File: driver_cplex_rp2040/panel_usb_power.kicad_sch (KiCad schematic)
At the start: 7 parts, among them J5 USB_C_Receptacle_USB2.0, U2 AP2112K-3.3

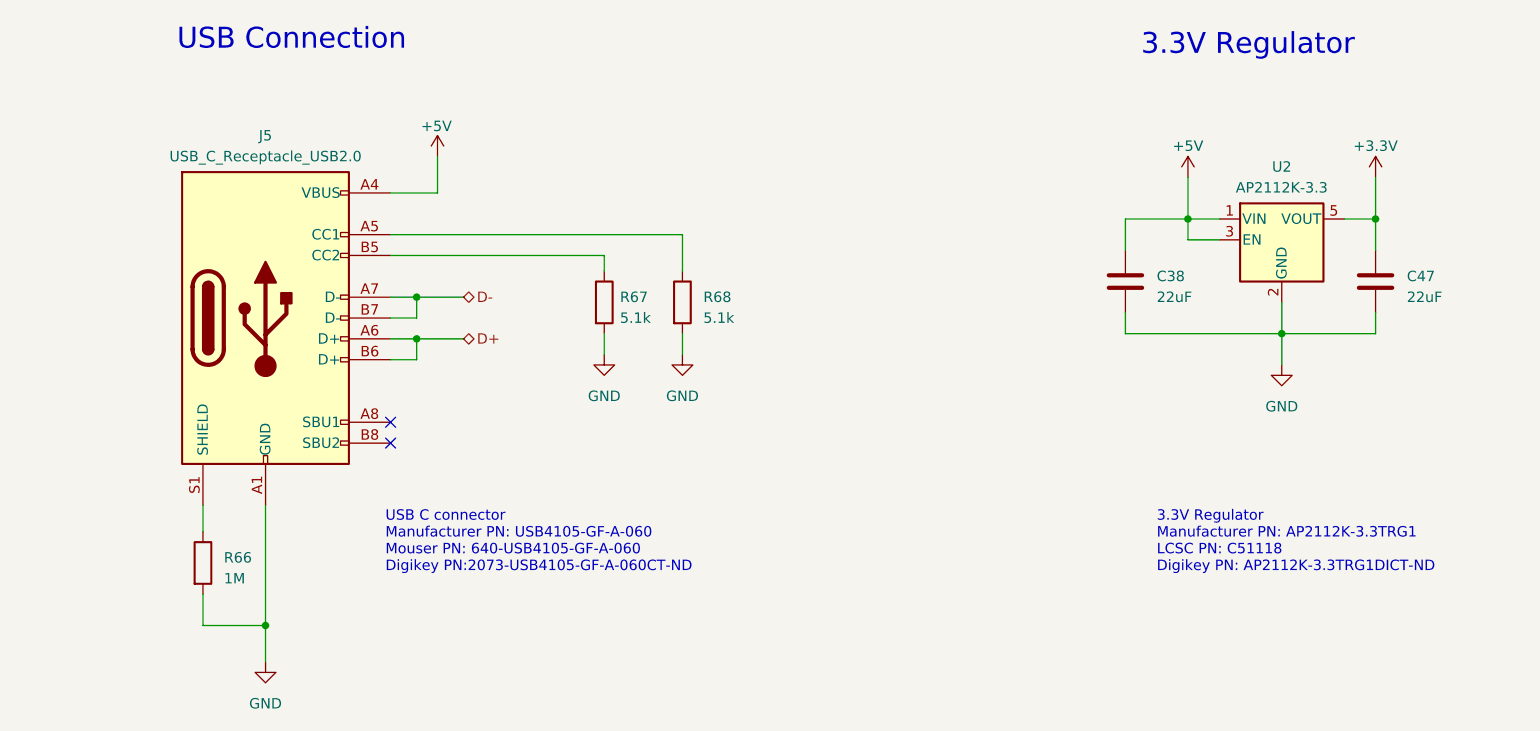
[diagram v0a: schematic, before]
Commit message: Added Charlieplexed version of rp2040 single pcb design.
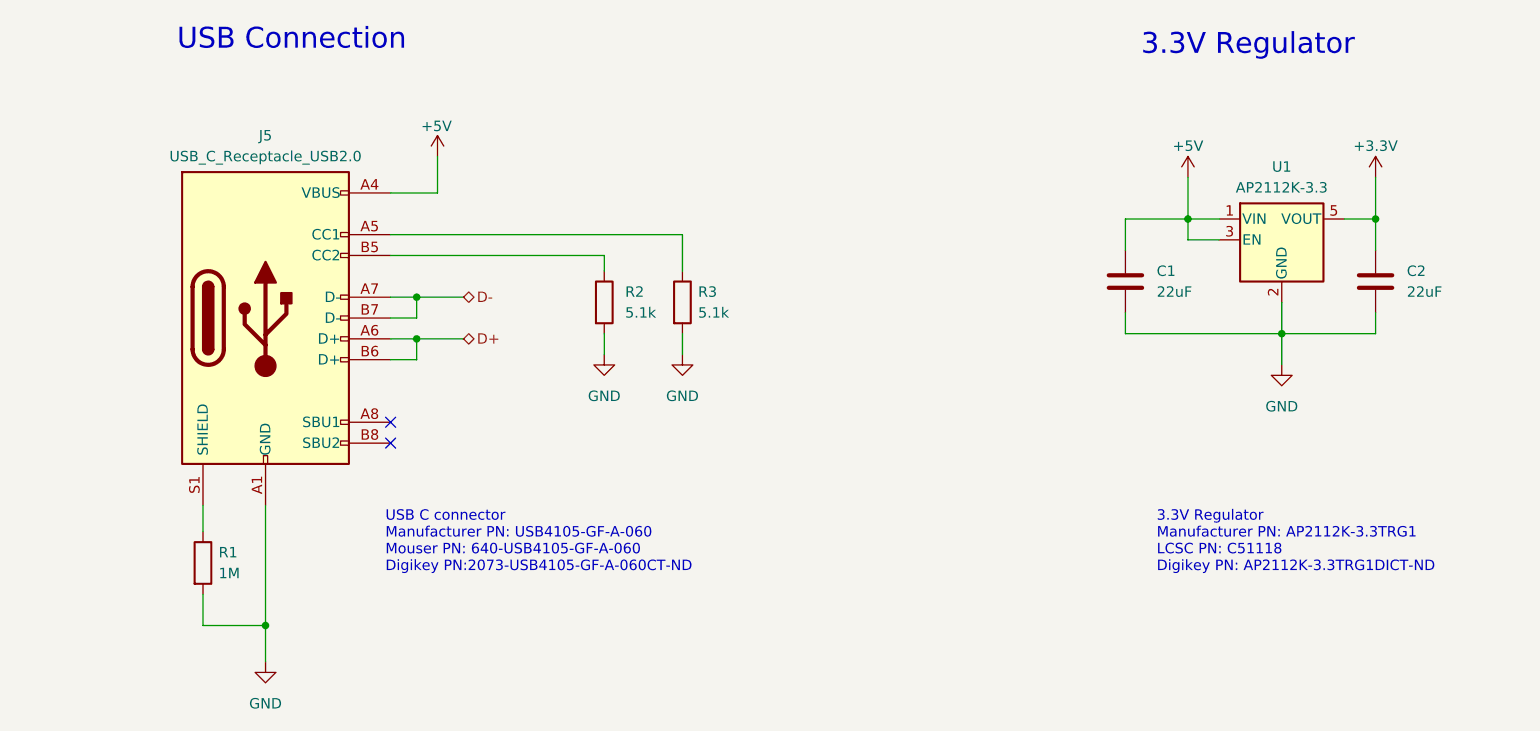
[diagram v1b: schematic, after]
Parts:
- renumbered C38 to C1, C47 to C2, R66 to R1, R67 to R2, R68 to R3, U2 to U1
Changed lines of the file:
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@@
   (symbol (lib_id "power:GND") (at 121.92 69.85 0) (unit 1)
     (in_bom yes) (on_board yes) (dnp no) (fields_autoplaced)
-    (property "Reference" "#PWR078" (at 121.92 76.2 0)
+    (property "Reference" "#PWR077" (at 121.92 76.2 0)
       (effects (font (size 1.27 1.27)) hide)
     )
@@
     (instances
       (project "driver_cplex_rp2040"
-        (path "/1e634561-32a0-4ffa-9d4f-e93f355464d5"
-          (reference "#PWR078") (unit 1)
-        )
         (path "/1e634561-32a0-4ffa-9d4f-e93f355464d5/e614504e-e15b-412a-a899-de4ba0827a39"
           (reference "#PWR077") (unit 1)
@@
   (symbol (lib_id "power:+3.3V") (at 215.9 48.26 0) (mirror y) (unit 1)
     (in_bom yes) (on_board yes) (dnp no) (fields_autoplaced)
-    (property "Reference" "#PWR076" (at 215.9 52.07 0)
+    (property "Reference" "#PWR075" (at 215.9 52.07 0)
       (effects (font (size 1.27 1.27)) hide)
     )
@@
     (instances
       (project "driver_cplex_rp2040"
-        (path "/1e634561-32a0-4ffa-9d4f-e93f355464d5"
-          (reference "#PWR076") (unit 1)
-        )
         (path "/1e634561-32a0-4ffa-9d4f-e93f355464d5/e614504e-e15b-412a-a899-de4ba0827a39"
           (reference "#PWR075") (unit 1)
@@
     (instances
       (project "driver_cplex_rp2040"
-        (path "/1e634561-32a0-4ffa-9d4f-e93f355464d5"
+        (path "/1e634561-32a0-4ffa-9d4f-e93f355464d5/e614504e-e15b-412a-a899-de4ba0827a39"
           (reference "#PWR018") (unit 1)
         )
-        (path "/1e634561-32a0-4ffa-9d4f-e93f355464d5/e614504e-e15b-412a-a899-de4ba0827a39"
-          (reference "#PWR018") (unit 1)
-        )
       )
     )
@@
   (symbol (lib_id "power:GND") (at 80.645 107.315 0) (unit 1)
     (in_bom yes) (on_board yes) (dnp no) (fields_autoplaced)
-    (property "Reference" "#PWR077" (at 80.645 113.665 0)
+    (property "Reference" "#PWR079" (at 80.645 113.665 0)
       (effects (font (size 1.27 1.27)) hide)
     )
@@
     (instances
       (project "driver_cplex_rp2040"
-        (path "/1e634561-32a0-4ffa-9d4f-e93f355464d5"
-          (reference "#PWR077") (unit 1)
-        )
         (path "/1e634561-32a0-4ffa-9d4f-e93f355464d5/e614504e-e15b-412a-a899-de4ba0827a39"
           (reference "#PWR079") (unit 1)
@@
     (instances
       (project "driver_cplex_rp2040"
-        (path "/1e634561-32a0-4ffa-9d4f-e93f355464d5"
+        (path "/1e634561-32a0-4ffa-9d4f-e93f355464d5/e614504e-e15b-412a-a899-de4ba0827a39"
           (reference "#PWR074") (unit 1)
         )
-        (path "/1e634561-32a0-4ffa-9d4f-e93f355464d5/e614504e-e15b-412a-a899-de4ba0827a39"
-          (reference "#PWR074") (unit 1)
-        )
       )
     )
@@
   (symbol (lib_id "Device:R") (at 121.92 63.5 0) (unit 1)
     (in_bom yes) (on_board yes) (dnp no) (fields_autoplaced)
-    (property "Reference" "R67" (at 123.825 62.865 0)
-      (effects (font (size 1.27 1.27)) (justify left))
-    )
-    (property "Value" "5.1k" (at 123.825 65.405 0)
+    (property "Reference" "R2" (at 124.46 62.23 0)
+      (effects (font (size 1.27 1.27)) (justify left))
+    )
+    (property "Value" "5.1k" (at 124.46 64.77 0)
       (effects (font (size 1.27 1.27)) (justify left))
     )
@@
     (instances
       (project "driver_cplex_rp2040"
-        (path "/1e634561-32a0-4ffa-9d4f-e93f355464d5"
-          (reference "R67") (unit 1)
-        )
-        (path "/1e634561-32a0-4ffa-9d4f-e93f355464d5/e614504e-e15b-412a-a899-de4ba0827a39"
-          (reference "R67") (unit 1)
+        (path "/1e634561-32a0-4ffa-9d4f-e93f355464d5/e614504e-e15b-412a-a899-de4ba0827a39"
+          (reference "R2") (unit 1)
         )
       )
@@
   (symbol (lib_id "Device:C") (at 185.42 60.96 0) (unit 1)
     (in_bom yes) (on_board yes) (dnp no) (fields_autoplaced)
-    (property "Reference" "C38" (at 189.23 60.325 0)
-      (effects (font (size 1.27 1.27)) (justify left))
-    )
-    (property "Value" "22uF" (at 189.23 62.865 0)
+    (property "Reference" "C1" (at 189.23 59.69 0)
+      (effects (font (size 1.27 1.27)) (justify left))
+    )
+    (property "Value" "22uF" (at 189.23 62.23 0)
       (effects (font (size 1.27 1.27)) (justify left))
     )
@@
     (instances
       (project "driver_cplex_rp2040"
-        (path "/1e634561-32a0-4ffa-9d4f-e93f355464d5"
-          (reference "C38") (unit 1)
-        )
-        (path "/1e634561-32a0-4ffa-9d4f-e93f355464d5/e614504e-e15b-412a-a899-de4ba0827a39"
-          (reference "C38") (unit 1)
+        (path "/1e634561-32a0-4ffa-9d4f-e93f355464d5/e614504e-e15b-412a-a899-de4ba0827a39"
+          (reference "C1") (unit 1)
         )
       )
@@
   (symbol (lib_id "Device:C") (at 215.9 60.96 0) (unit 1)
     (in_bom yes) (on_board yes) (dnp no) (fields_autoplaced)
-    (property "Reference" "C47" (at 219.71 60.325 0)
-      (effects (font (size 1.27 1.27)) (justify left))
-    )
-    (property "Value" "22uF" (at 219.71 62.865 0)
+    (property "Reference" "C2" (at 219.71 59.69 0)
+      (effects (font (size 1.27 1.27)) (justify left))
+    )
+    (property "Value" "22uF" (at 219.71 62.23 0)
       (effects (font (size 1.27 1.27)) (justify left))
     )
@@
     (instances
       (project "driver_cplex_rp2040"
-        (path "/1e634561-32a0-4ffa-9d4f-e93f355464d5"
-          (reference "C47") (unit 1)
-        )
-        (path "/1e634561-32a0-4ffa-9d4f-e93f355464d5/e614504e-e15b-412a-a899-de4ba0827a39"
-          (reference "C47") (unit 1)
+        (path "/1e634561-32a0-4ffa-9d4f-e93f355464d5/e614504e-e15b-412a-a899-de4ba0827a39"
+          (reference "C2") (unit 1)
         )
       )
@@
   (symbol (lib_id "Regulator_Linear:AP2112K-3.3") (at 204.47 55.88 0) (unit 1)
     (in_bom yes) (on_board yes) (dnp no) (fields_autoplaced)
-    (property "Reference" "U2" (at 204.47 46.99 0)
+    (property "Reference" "U1" (at 204.47 46.99 0)
       (effects (font (size 1.27 1.27)))
     )
@@
     (instances
       (project "driver_cplex_rp2040"
-        (path "/1e634561-32a0-4ffa-9d4f-e93f355464d5"
-          (reference "U2") (unit 1)
-        )
-        (path "/1e634561-32a0-4ffa-9d4f-e93f355464d5/e614504e-e15b-412a-a899-de4ba0827a39"
-          (reference "U2") (unit 1)
+        (path "/1e634561-32a0-4ffa-9d4f-e93f355464d5/e614504e-e15b-412a-a899-de4ba0827a39"
+          (reference "U1") (unit 1)
         )
       )
@@
   (symbol (lib_id "power:GND") (at 204.47 71.12 0) (unit 1)
     (in_bom yes) (on_board yes) (dnp no) (fields_autoplaced)
-    (property "Reference" "#PWR075" (at 204.47 77.47 0)
+    (property "Reference" "#PWR076" (at 204.47 77.47 0)
       (effects (font (size 1.27 1.27)) hide)
     )
@@
     (instances
       (project "driver_cplex_rp2040"
-        (path "/1e634561-32a0-4ffa-9d4f-e93f355464d5"
-          (reference "#PWR075") (unit 1)
-        )
         (path "/1e634561-32a0-4ffa-9d4f-e93f355464d5/e614504e-e15b-412a-a899-de4ba0827a39"
           (reference "#PWR076") (unit 1)
@@
   (symbol (lib_id "Device:R") (at 73.025 95.25 0) (unit 1)
     (in_bom yes) (on_board yes) (dnp no) (fields_autoplaced)
-    (property "Reference" "R66" (at 75.565 94.615 0)
-      (effects (font (size 1.27 1.27)) (justify left))
-    )
-    (property "Value" "1M" (at 75.565 97.155 0)
+    (property "Reference" "R1" (at 74.93 93.98 0)
+      (effects (font (size 1.27 1.27)) (justify left))
+    )
+    (property "Value" "1M" (at 74.93 96.52 0)
       (effects (font (size 1.27 1.27)) (justify left))
     )
@@
     (instances
       (project "driver_cplex_rp2040"
-        (path "/1e634561-32a0-4ffa-9d4f-e93f355464d5"
-          (reference "R66") (unit 1)
-        )
-        (path "/1e634561-32a0-4ffa-9d4f-e93f355464d5/e614504e-e15b-412a-a899-de4ba0827a39"
-          (reference "R66") (unit 1)
+        (path "/1e634561-32a0-4ffa-9d4f-e93f355464d5/e614504e-e15b-412a-a899-de4ba0827a39"
+          (reference "R1") (unit 1)
         )
       )
@@
   (symbol (lib_id "power:GND") (at 131.445 69.85 0) (unit 1)
     (in_bom yes) (on_board yes) (dnp no) (fields_autoplaced)
-    (property "Reference" "#PWR079" (at 131.445 76.2 0)
+    (property "Reference" "#PWR078" (at 131.445 76.2 0)
       (effects (font (size 1.27 1.27)) hide)
     )
@@
     (instances
       (project "driver_cplex_rp2040"
-        (path "/1e634561-32a0-4ffa-9d4f-e93f355464d5"
-          (reference "#PWR079") (unit 1)
-        )
         (path "/1e634561-32a0-4ffa-9d4f-e93f355464d5/e614504e-e15b-412a-a899-de4ba0827a39"
           (reference "#PWR078") (unit 1)
@@
     (instances
       (project "driver_cplex_rp2040"
-        (path "/1e634561-32a0-4ffa-9d4f-e93f355464d5"
+        (path "/1e634561-32a0-4ffa-9d4f-e93f355464d5/e614504e-e15b-412a-a899-de4ba0827a39"
           (reference "J5") (unit 1)
         )
-        (path "/1e634561-32a0-4ffa-9d4f-e93f355464d5/e614504e-e15b-412a-a899-de4ba0827a39"
-          (reference "J5") (unit 1)
-        )
       )
     )
@@
   (symbol (lib_id "Device:R") (at 131.445 63.5 0) (unit 1)
     (in_bom yes) (on_board yes) (dnp no) (fields_autoplaced)
-    (property "Reference" "R68" (at 133.985 62.865 0)
-      (effects (font (size 1.27 1.27)) (justify left))
-    )
-    (property "Value" "5.1k" (at 133.985 65.405 0)
+    (property "Reference" "R3" (at 133.35 62.23 0)
+      (effects (font (size 1.27 1.27)) (justify left))
+    )
+    (property "Value" "5.1k" (at 133.35 64.77 0)
       (effects (font (size 1.27 1.27)) (justify left))
     )
@@
     (instances
       (project "driver_cplex_rp2040"
-        (path "/1e634561-32a0-4ffa-9d4f-e93f355464d5"
-          (reference "R68") (unit 1)
-        )
-        (path "/1e634561-32a0-4ffa-9d4f-e93f355464d5/e614504e-e15b-412a-a899-de4ba0827a39"
-          (reference "R68") (unit 1)
-        )
-      )
+        (path "/1e634561-32a0-4ffa-9d4f-e93f355464d5/e614504e-e15b-412a-a899-de4ba0827a39"
+          (reference "R3") (unit 1)
+        )
+      )

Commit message: Worked on footprint assignment for rp2040 single panel cplex design.
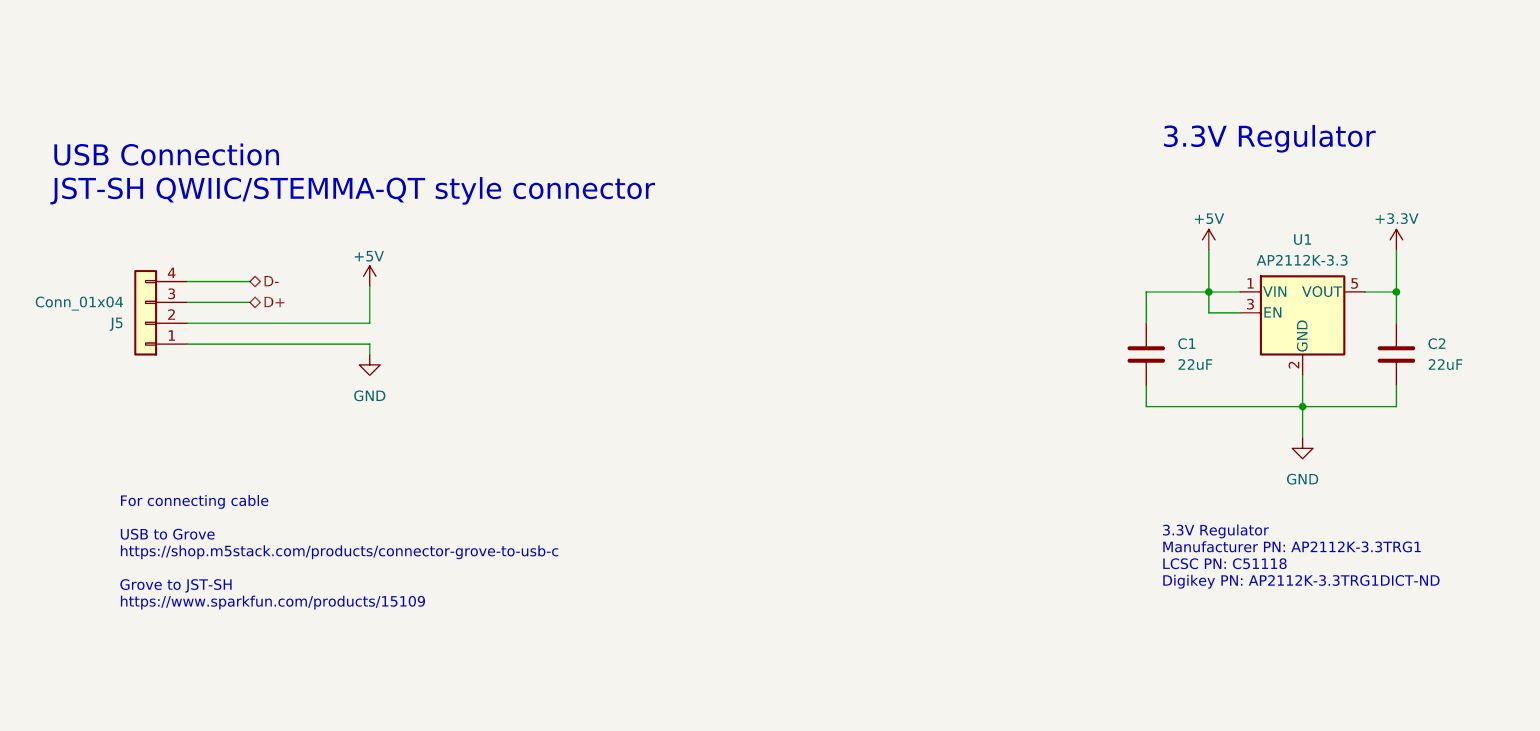
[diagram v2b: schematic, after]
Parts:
- removed J5: USB_C_Receptacle_USB2.0, Connector_USB:USB_C_Receptacle_G-Switch_GT-USB-7010ASV, symbol Connector:USB_C_Receptacle_USB2.0
- removed R1: 1M, symbol Device:R
- removed R2, R3: 5.1k, symbol Device:R
- added J5: Conn_01x04, symbol Connector_Generic:Conn_01x04
- C1, C2: footprint panel_custom:C_0201_0603Metric -> panel_custom:C_0402_1005Metric
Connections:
- net +5V: now also J5.2 (Pin_2)
- net D+: now also J5.3 (Pin_3)
- net D-: now also J5.4 (Pin_4)
- net GND: now also J5.1 (Pin_1)
- no-connect marks 2 -> 0
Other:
- note added: "For connecting cable USB to Grove https://shop.m5stack.com/products/connector-grove-to-usb-c Grove to JST-SH https://www.sparkfun.com/products/15109"
- note added: "USB Connection JST-SH QWIIC/STEMMA-QT style connector"
- note removed: "USB C connector Manufacturer PN: USB4105-GF-A-060 Mouser PN: 640-USB4105-GF-A-060 Digikey PN:2073-USB4105-GF-A-060CT-ND"
- note removed: "USB Connection"
- moved on the sheet: C1, C2, U1

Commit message: Worked on layout.
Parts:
- J5: footprint (none) -> panel_custom:JST_SH_SM04B-SRSS-TB_1x04-1MP_P1.00mm_Horizontal
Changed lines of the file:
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@@
       (effects (font (size 1.27 1.27)) (justify left))
     )
-    (property "Footprint" "" (at 66.04 66.04 0)
+    (property "Footprint" "panel_custom:JST_SH_SM04B-SRSS-TB_1x04-1MP_P1.00mm_Horizontal" (at 66.04 66.04 0)
       (effects (font (size 1.27 1.27)) hide)
     )

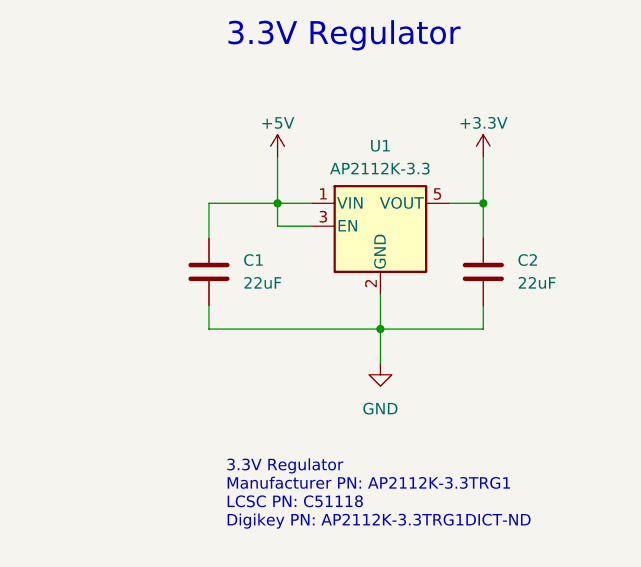
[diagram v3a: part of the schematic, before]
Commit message: Work on rp2040 cplex'd design routing and layout.
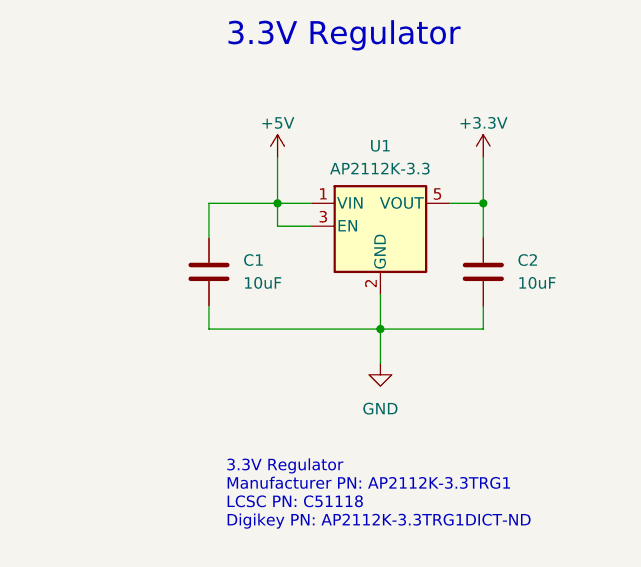
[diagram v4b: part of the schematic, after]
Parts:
- C1, C2: value 22uF -> 10uF
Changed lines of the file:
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@@
       (effects (font (size 1.27 1.27)) (justify left))
     )
-    (property "Value" "22uF" (at 191.77 71.12 0)
+    (property "Value" "10uF" (at 191.77 71.12 0)
       (effects (font (size 1.27 1.27)) (justify left))
     )
@@
       (effects (font (size 1.27 1.27)) (justify left))
     )
-    (property "Value" "22uF" (at 222.25 71.12 0)
+    (property "Value" "10uF" (at 222.25 71.12 0)
       (effects (font (size 1.27 1.27)) (justify left))
     )
